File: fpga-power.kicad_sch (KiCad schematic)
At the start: 100 parts, among them U15 XC7K160T-FFG676

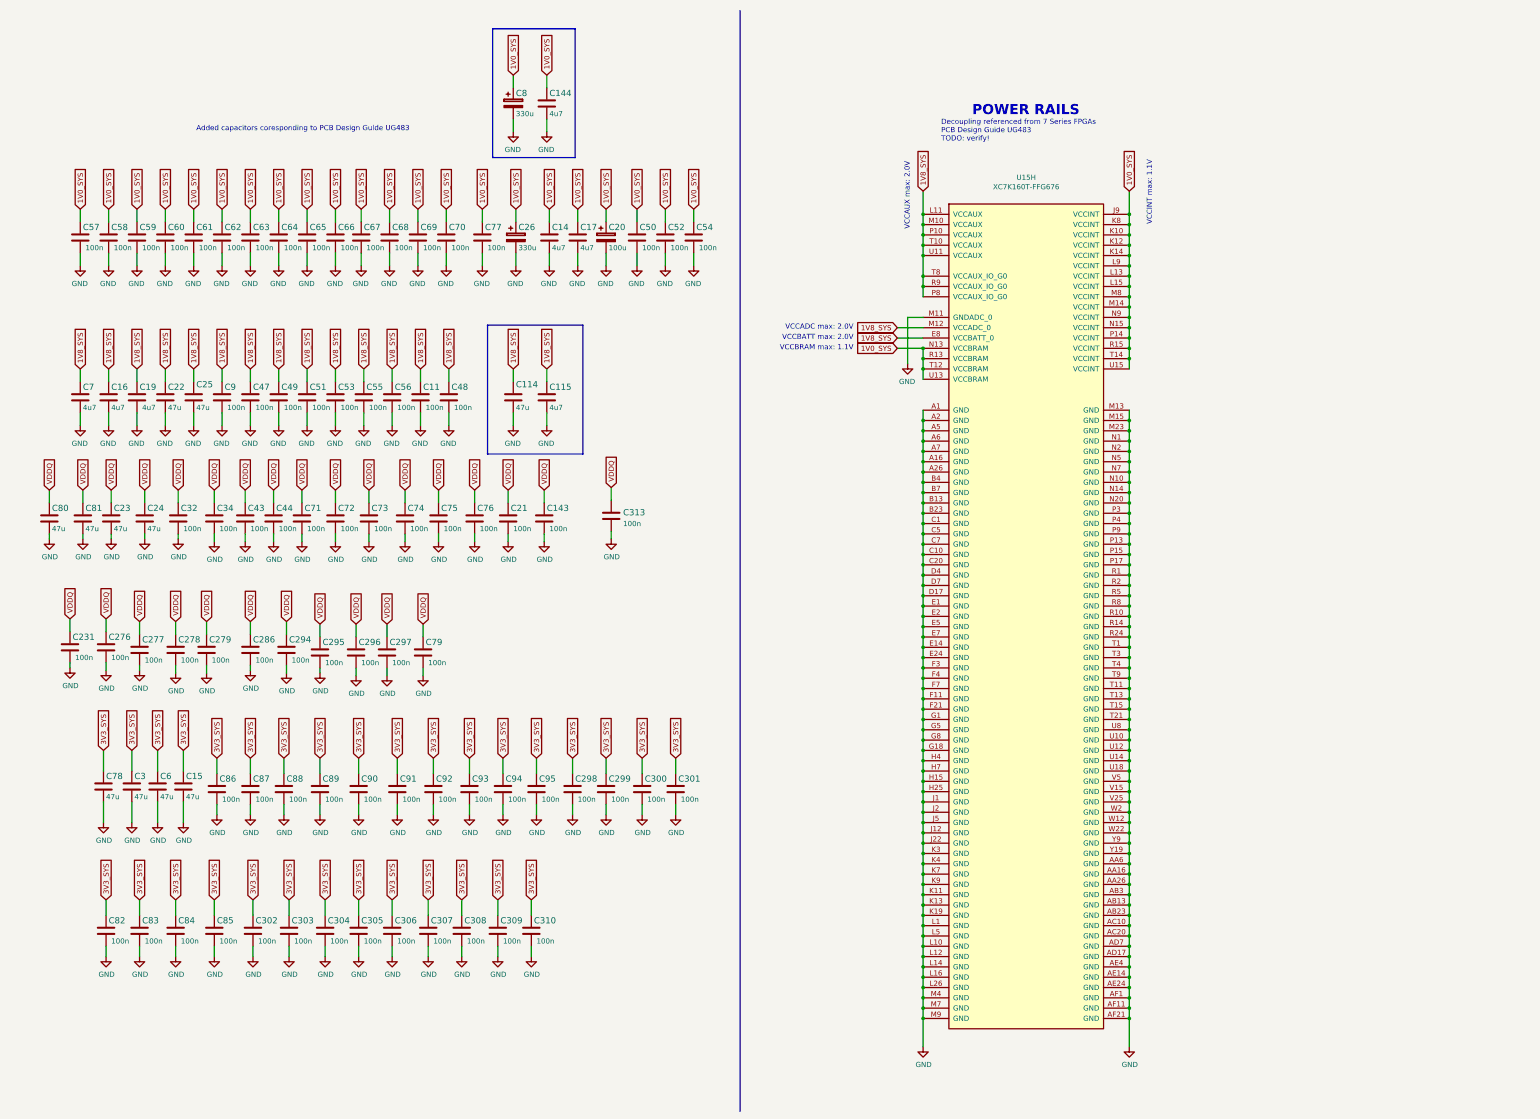
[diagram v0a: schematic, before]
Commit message: Rebase to Rev. 1.2.2
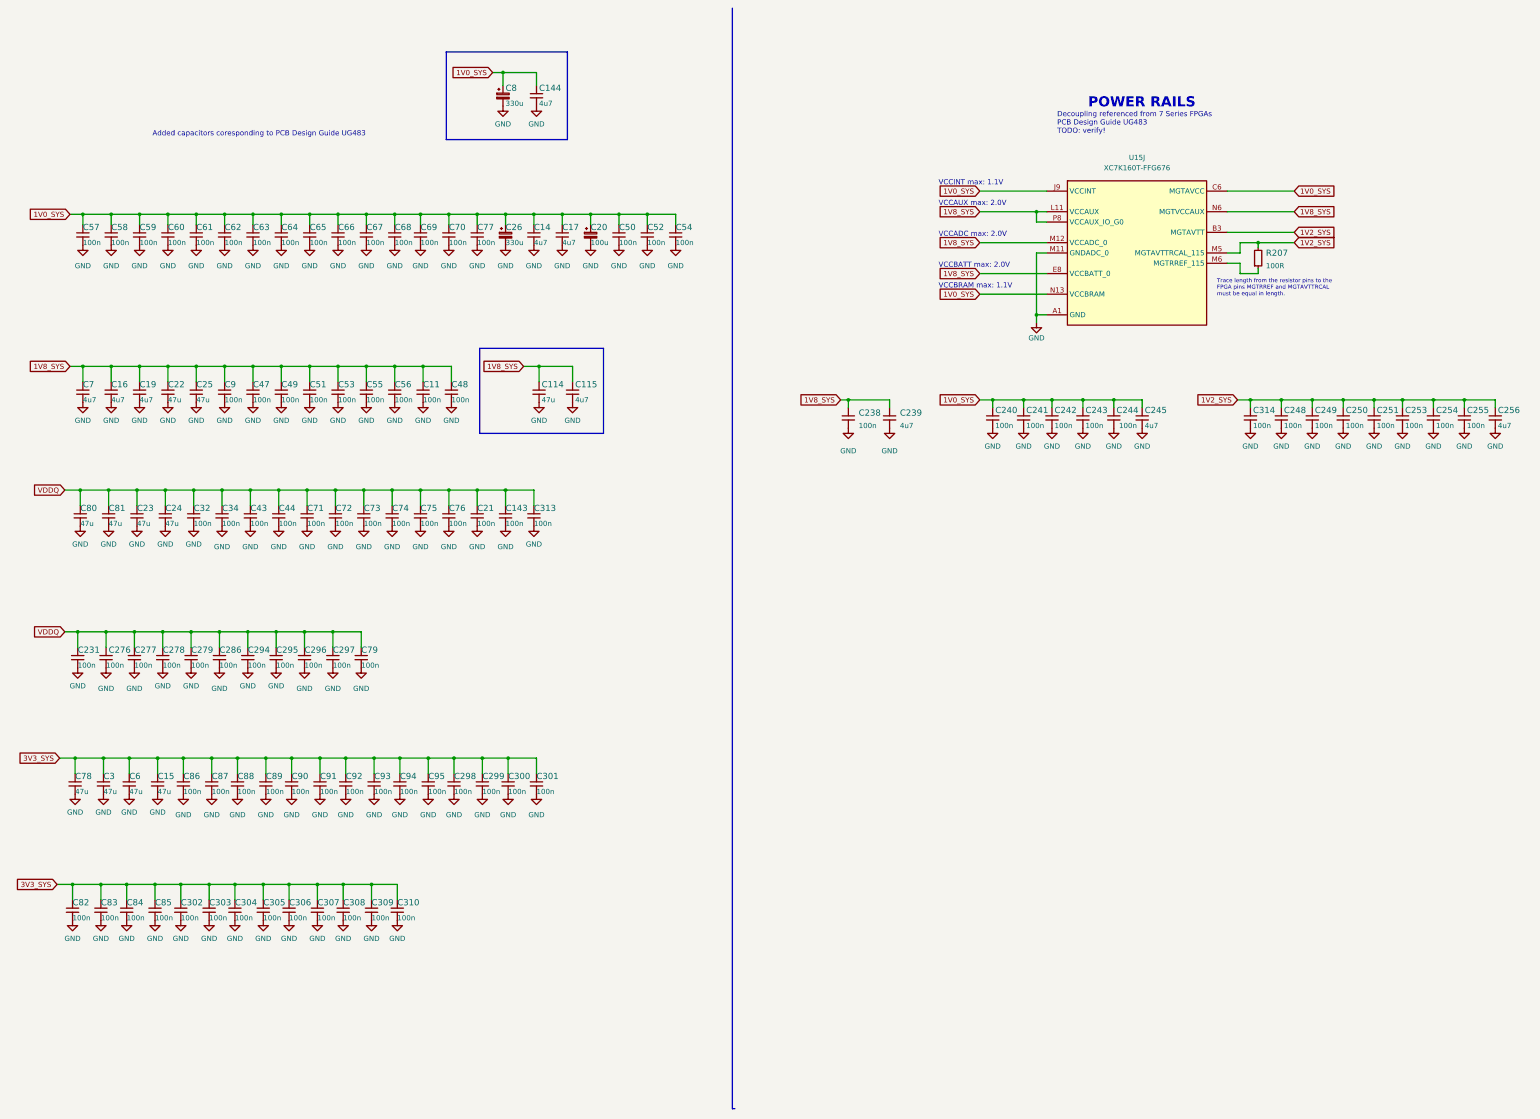
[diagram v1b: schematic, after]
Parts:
- removed C11, C143, C21, C231, C276, C277, C278, C279, C286, C294, C295, C296, C297, C298, C299, C300, C301, C302, C303, C304, C305, C306, C307, C308, C309, C310, C32, C34, C43, C44, C47, C48, C49, C50, C51, C52, C53, C54, C55, C56, C57, C58, C59, C60, C61, C62, C63, C64, C65, C66, C67, C68, C69, C70, C71, C72, C73, C74, C75, C76, C77, C79, C82, C83, C84, C85, C86, C87, C88, C89, C9, C90, C91, C92, C93, C94, C95: C_100n_0201, data-center-dram-tester-footprints:0201-res, symbol data-center-dram-tester:C_100n_0201
- removed C114, C15, C22, C23, C24, C25, C3, C6, C78, C80, C81: C_47u_0603, data-center-dram-tester-footprints:0603-cap, symbol data-center-dram-tester:C_47u_0603
- removed C115, C14, C144, C16, C17, C19, C7: C_4u7_0402, data-center-dram-tester-footprints:0402-cap, symbol data-center-dram-tester:C_4u7_0402
- removed C20: C_100u_KEMET_A, antmicro-footprints:KEMET_A, symbol data-center-dram-tester:C_100u_KEMET_A
- removed C26, C8: C_330u_KEMET_D, data-center-dram-tester-footprints:KEMET_D, symbol data-center-dram-tester:C_330u_KEMET_D
- removed C313: C_100n_0402, antmicro-footprints:0402-cap, symbol antmicroCapacitors0402:C_100n_0402
- removed U15: XC7K160T-FFG676, antmicro-footprints:xc7k160tfbg676, symbol data-center-dram-tester:XC7K160T-FFG676
- added C11, C143, C21, C231, C238, C240, C241, C242, C243, C244, C248, C249, C250, C251, C253, C254, C255, C276, C277, C278, C279, C286, C294, C295, C296, C297, C298, C299, C300, C301, C302, C303, C304, C305, C306, C307, C308, C309, C310, C32, C34, C43, C44, C47, C48, C49, C50, C51, C52, C53, C54, C55, C56, C57, C58, C59, C60, C61, C62, C63, C64, C65, C66, C67, C68, C69, C70, C71, C72, C73, C74, C75, C76, C77, C79, C82, C83, C84, C85, C86, C87, C88, C89, C9, C90, C91, C92, C93, C94, C95: C_100n_0201, data-center-rdimm-ddr4-tester-footprints:C_0201, symbol data-center-rdimm-ddr4-tester:C_100n_0201
- added C114, C15, C22, C23, C24, C25, C3, C6, C78, C80, C81: C_47u_0603, data-center-rdimm-ddr4-tester-footprints:C_0603_1608Metric, symbol data-center-rdimm-ddr4-tester:C_47u_0603
- added C115, C14, C144, C16, C17, C19, C239, C245, C256, C7: C_4u7_0402, data-center-rdimm-ddr4-tester-footprints:C_0402_1005Metric, symbol data-center-rdimm-ddr4-tester:C_4u7_0402
- added C20: C_100u_KEMET_A, data-center-rdimm-ddr4-tester-footprints:KEMET_A, symbol data-center-rdimm-ddr4-tester:C_100u_KEMET_A
- added C26, C8: C_330u_KEMET_D, data-center-rdimm-ddr4-tester-footprints:KEMET_D, symbol data-center-rdimm-ddr4-tester:C_330u_KEMET_D
- added C313, C314: C_100n_0402, data-center-rdimm-ddr4-tester-footprints:C_0402_1005Metric, symbol data-center-rdimm-ddr4-tester:C_100n_0402
- added R207: R_100R_0402, data-center-rdimm-ddr4-tester-footprints:R_0402_1005Metric, symbol data-center-rdimm-ddr4-tester:R_100R_0402
- added U15: XC7K160T-FFG676, data-center-rdimm-ddr4-tester-footprints:BGA-676_27x27mm_Layout26x26_P1X1mm, symbol data-center-rdimm-ddr4-tester:XC7K160T-FFG676
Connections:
- net 1V0_SYS: now also C14.1, C144.1, C17.1, C20.1, C240.1, C241.1, C242.1, C243.1, C244.1, C245.1, C26.1, C50.1, C52.1, C54.1, C57.1, C58.1, C59.1, C60.1, C61.1, C62.1, C63.1, C64.1, C65.1, C66.1, C67.1, C68.1, C69.1, C70.1, C77.1, C8.1, U15.C6 (MGTAVCC), U15.E6 (MGTAVCC), U15.G6 (MGTAVCC), U15.J6 (MGTAVCC), U15.J9 (VCCINT), U15.K10 (VCCINT), U15.K12 (VCCINT), U15.K14 (VCCINT), U15.K8 (VCCINT), U15.L13 (VCCINT), U15.L15 (VCCINT), U15.L6 (MGTAVCC), U15.L9 (VCCINT), U15.M14 (VCCINT), U15.M8 (VCCINT), U15.N13 (VCCBRAM), U15.N15 (VCCINT), U15.N9 (VCCINT), U15.P14 (VCCINT), U15.R13 (VCCBRAM), U15.R15 (VCCINT), U15.T12 (VCCBRAM), U15.T14 (VCCINT), U15.U13 (VCCBRAM), U15.U15 (VCCINT)
- net 1V8_SYS: now also C11.1, C114.1, C115.1, C16.1, C19.1, C22.1, C238.1, C239.1, C25.1, C47.1, C48.1, C49.1, C51.1, C53.1, C55.1, C56.1, C7.1, C9.1, U15.E8 (VCCBATT_0), U15.L11 (VCCAUX), U15.M10 (VCCAUX), U15.M12 (VCCADC_0), U15.N6 (MGTVCCAUX), U15.P10 (VCCAUX), U15.P8 (VCCAUX_IO_G0), U15.R9 (VCCAUX_IO_G0), U15.T10 (VCCAUX), U15.T8 (VCCAUX_IO_G0), U15.U11 (VCCAUX)
- net 3V3_SYS: now also C15.1, C298.1, C299.1, C3.1, C300.1, C301.1, C302.1, C303.1, C304.1, C305.1, C306.1, C307.1, C308.1, C309.1, C310.1, C6.1, C78.1, C82.1, C83.1, C84.1, C85.1, C86.1, C87.1, C88.1, C89.1, C90.1, C91.1, C92.1, C93.1, C94.1, C95.1
- net GND: now also C11.2, C114.2, C115.2, C14.2, C143.2, C144.2, C15.2, C16.2, C17.2, C19.2, C20.2, C21.2, C22.2, C23.2, C231.2, C238.2, C239.2, C24.2, C240.2, C241.2, C242.2, C243.2, C244.2, C245.2, C248.2, C249.2, C25.2, C250.2, C251.2, C253.2, C254.2, C255.2, C256.2, C26.2, C276.2, C277.2, C278.2, C279.2, C286.2, C294.2, C295.2, C296.2, C297.2, C298.2, C299.2, C3.2, C300.2, C301.2, C302.2, C303.2, C304.2, C305.2, C306.2, C307.2, C308.2, C309.2, C310.2, C313.2, C314.2, C32.2, C34.2, C43.2, C44.2, C47.2, C48.2, C49.2, C50.2, C51.2, C52.2, C53.2, C54.2, C55.2, C56.2, C57.2, C58.2, C59.2, C6.2, C60.2, C61.2, C62.2, C63.2, C64.2, C65.2, C66.2, C67.2, C68.2, C69.2, C7.2, C70.2, C71.2, C72.2, C73.2, C74.2, C75.2, C76.2, C77.2, C78.2, C79.2, C8.2, C80.2, C81.2, C82.2, C83.2, C84.2, C85.2, C86.2, C87.2, C88.2, C89.2, C9.2, C90.2, C91.2, C92.2, C93.2, C94.2, C95.2, U15.A1 (GND), U15.A16 (GND), U15.A2 (GND), U15.A26 (GND), U15.A5 (GND), U15.A6 (GND), U15.A7 (GND), U15.AA16 (GND), U15.AA26 (GND), U15.AA6 (GND), U15.AB13 (GND), U15.AB23 (GND), U15.AB3 (GND), U15.AC10 (GND), U15.AC20 (GND), U15.AD17 (GND), U15.AD7 (GND), U15.AE14 (GND), U15.AE24 (GND), U15.AE4 (GND), U15.AF1 (GND), U15.AF11 (GND), U15.AF21 (GND), U15.B13 (GND), U15.B23 (GND), U15.B4 (GND), U15.B7 (GND), U15.C1 (GND), U15.C10 (GND), U15.C20 (GND), U15.C5 (GND), U15.C7 (GND), U15.D17 (GND), U15.D4 (GND), U15.D7 (GND), U15.E1 (GND), U15.E14 (GND), U15.E2 (GND), U15.E24 (GND), U15.E5 (GND), U15.E7 (GND), U15.F11 (GND), U15.F21 (GND), U15.F3 (GND), U15.F4 (GND), U15.F7 (GND), U15.G1 (GND), U15.G18 (GND), U15.G5 (GND), U15.G8 (GND), U15.H15 (GND), U15.H25 (GND), U15.H4 (GND), U15.H7 (GND), U15.J1 (GND), U15.J12 (GND), U15.J2 (GND), U15.J22 (GND), U15.J5 (GND), U15.K11 (GND), U15.K13 (GND), U15.K19 (GND), U15.K3 (GND), U15.K4 (GND), U15.K7 (GND), U15.K9 (GND), U15.L1 (GND), U15.L10 (GND), U15.L12 (GND), U15.L14 (GND), U15.L16 (GND), U15.L26 (GND), U15.L5 (GND), U15.M11 (GNDADC_0), U15.M13 (GND), U15.M15 (GND), U15.M23 (GND), U15.M4 (GND), U15.M7 (GND), U15.M9 (GND), U15.N1 (GND), U15.N10 (GND), U15.N14 (GND), U15.N2 (GND), U15.N20 (GND), U15.N5 (GND), U15.N7 (GND), U15.P13 (GND), U15.P15 (GND), U15.P17 (GND), U15.P3 (GND), U15.P4 (GND), U15.P9 (GND), U15.R1 (GND), U15.R10 (GND), U15.R14 (GND), U15.R2 (GND), U15.R24 (GND), U15.R5 (GND), U15.R8 (GND), U15.T1 (GND), U15.T11 (GND), U15.T13 (GND), U15.T15 (GND), U15.T21 (GND), U15.T3 (GND), U15.T4 (GND), U15.T9 (GND), U15.U10 (GND), U15.U12 (GND), U15.U14 (GND), U15.U18 (GND), U15.U8 (GND), U15.V15 (GND), U15.V25 (GND), U15.V5 (GND), U15.W12 (GND), U15.W2 (GND), U15.W22 (GND), U15.Y19 (GND), U15.Y9 (GND)
- net VDDQ: now also C143.1, C21.1, C23.1, C231.1, C24.1, C276.1, C277.1, C278.1, C279.1, C286.1, C294.1, C295.1, C296.1, C297.1, C313.1, C32.1, C34.1, C43.1, C44.1, C71.1, C72.1, C73.1, C74.1, C75.1, C76.1, C79.1, C80.1, C81.1
- new net: R207.1, U15.M6 (MGTRREF_115)
- new net 1V2_SYS: C248.1, C249.1, C250.1, C251.1, C253.1, C254.1, C255.1, C256.1, C314.1, R207.2, U15.B3 (MGTAVTT), U15.C2 (MGTAVTT), U15.D3 (MGTAVTT), U15.G2 (MGTAVTT), U15.H3 (MGTAVTT), U15.L2 (MGTAVTT), U15.M3 (MGTAVTT), U15.M5 (MGTAVTTRCAL_115)
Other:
- note added: "Trace length from the resistor pins to the FPGA pins MGTRREF and MGTAVTTRCAL must be equal in length."

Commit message: Update designators and sync schematic with PCB
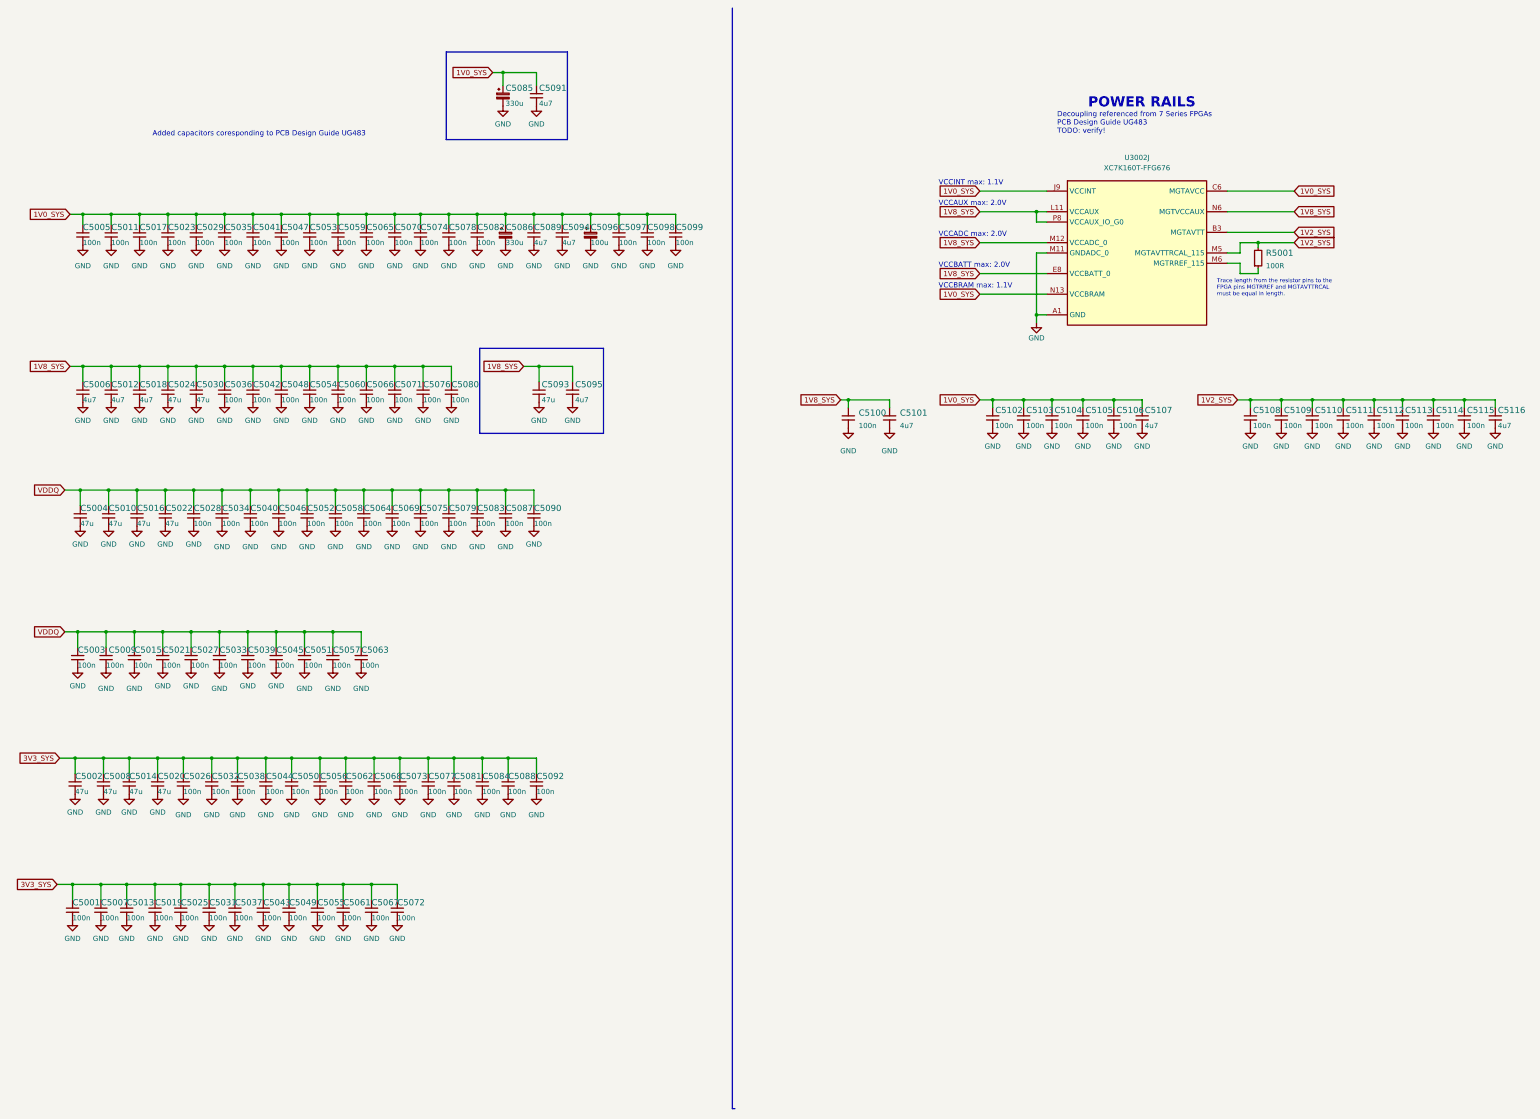
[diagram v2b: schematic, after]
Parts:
- renumbered C82 to C5001, C78 to C5002, C231 to C5003, C80 to C5004, C57 to C5005, C7 to C5006, C83 to C5007, C3 to C5008, C276 to C5009, C81 to C5010, C58 to C5011, C16 to C5012, C84 to C5013, C6 to C5014, C277 to C5015, C23 to C5016, C59 to C5017, C19 to C5018, C85 to C5019, C15 to C5020, C278 to C5021, C24 to C5022, C60 to C5023, C22 to C5024, C302 to C5025, C86 to C5026, C279 to C5027, C32 to C5028, C61 to C5029, C25 to C5030, C303 to C5031, C87 to C5032, C286 to C5033, C34 to C5034, C62 to C5035, C9 to C5036, C304 to C5037, C88 to C5038, C294 to C5039, C43 to C5040, C63 to C5041, C47 to C5042, C305 to C5043, C89 to C5044, C295 to C5045, C44 to C5046, C64 to C5047, C49 to C5048, C306 to C5049, C90 to C5050, C296 to C5051, C71 to C5052, C65 to C5053, C51 to C5054, C307 to C5055, C91 to C5056, C297 to C5057, C72 to C5058, C66 to C5059, C53 to C5060, C308 to C5061, C92 to C5062, C79 to C5063, C73 to C5064, C67 to C5065, C55 to C5066, C309 to C5067, C93 to C5068, C74 to C5069, C68 to C5070, C56 to C5071, C310 to C5072, C94 to C5073, C69 to C5074, C75 to C5075, C11 to C5076, C95 to C5077, C70 to C5078, C76 to C5079, C48 to C5080, C298 to C5081, C77 to C5082, C21 to C5083, C299 to C5084, C8 to C5085, C26 to C5086, C143 to C5087, C300 to C5088, C14 to C5089, C313 to C5090, C144 to C5091, C301 to C5092, C114 to C5093, C17 to C5094, C115 to C5095, C20 to C5096, C50 to C5097, C52 to C5098, C54 to C5099, C238 to C5100, C239 to C5101, C240 to C5102, C241 to C5103, C242 to C5104, C243 to C5105, C244 to C5106, C245 to C5107, C314 to C5108, C248 to C5109, C249 to C5110, C250 to C5111, C251 to C5112, C253 to C5113, C254 to C5114, C255 to C5115, C256 to C5116, R207 to R5001, U15 to U3002

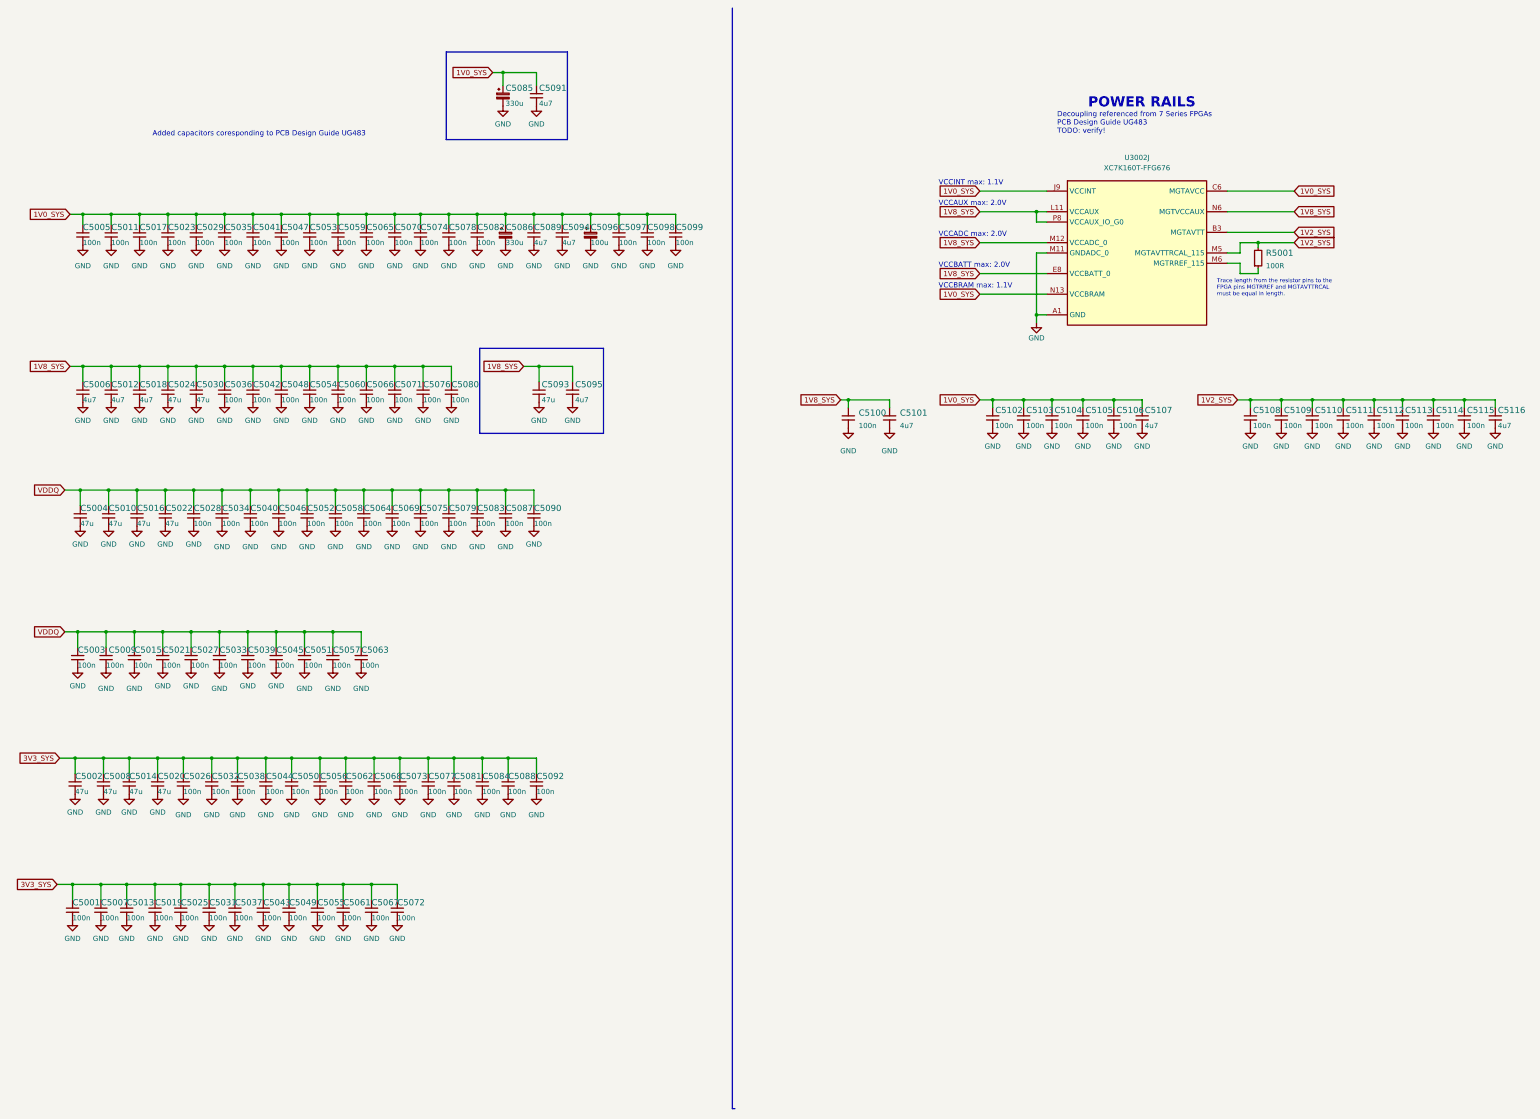
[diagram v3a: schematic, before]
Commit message: Replace supply labels with proper symbols
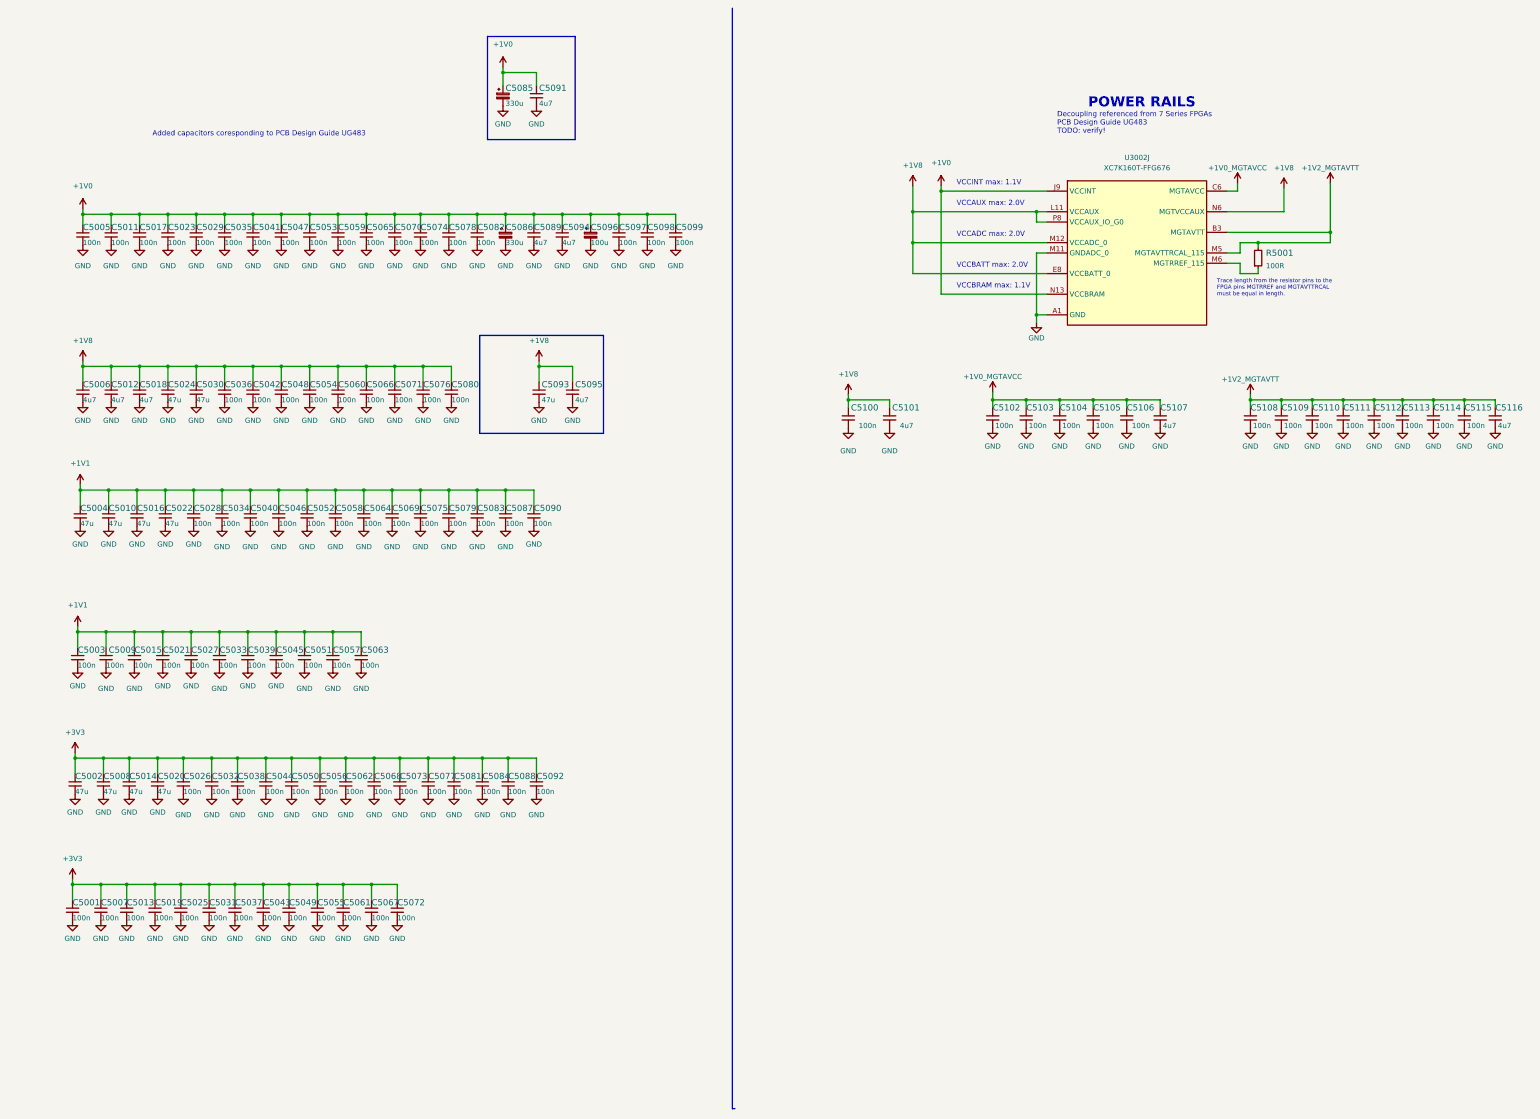
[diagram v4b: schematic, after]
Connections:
- net 1V0_SYS renamed +1V0
- net +1V0: no longer C5102.1, C5103.1, C5104.1, C5105.1, C5106.1, C5107.1, U3002.C6 (MGTAVCC), U3002.E6 (MGTAVCC), U3002.G6 (MGTAVCC), U3002.J6 (MGTAVCC), U3002.L6 (MGTAVCC)
- net 1V2_SYS renamed +1V2_MGTAVTT
- net 1V8_SYS renamed +1V8
- net 3V3_SYS renamed +3V3
- net VDDQ renamed +1V1
- new net +1V0_MGTAVCC: C5102.1, C5103.1, C5104.1, C5105.1, C5106.1, C5107.1, U3002.C6 (MGTAVCC), U3002.E6 (MGTAVCC), U3002.G6 (MGTAVCC), U3002.J6 (MGTAVCC), U3002.L6 (MGTAVCC)
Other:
- moved on the sheet: C5103, C5104, C5105, C5106, C5107
